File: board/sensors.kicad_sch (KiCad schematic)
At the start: 9 parts, among them J7 U.FL GPS, U7 MAX-M10M

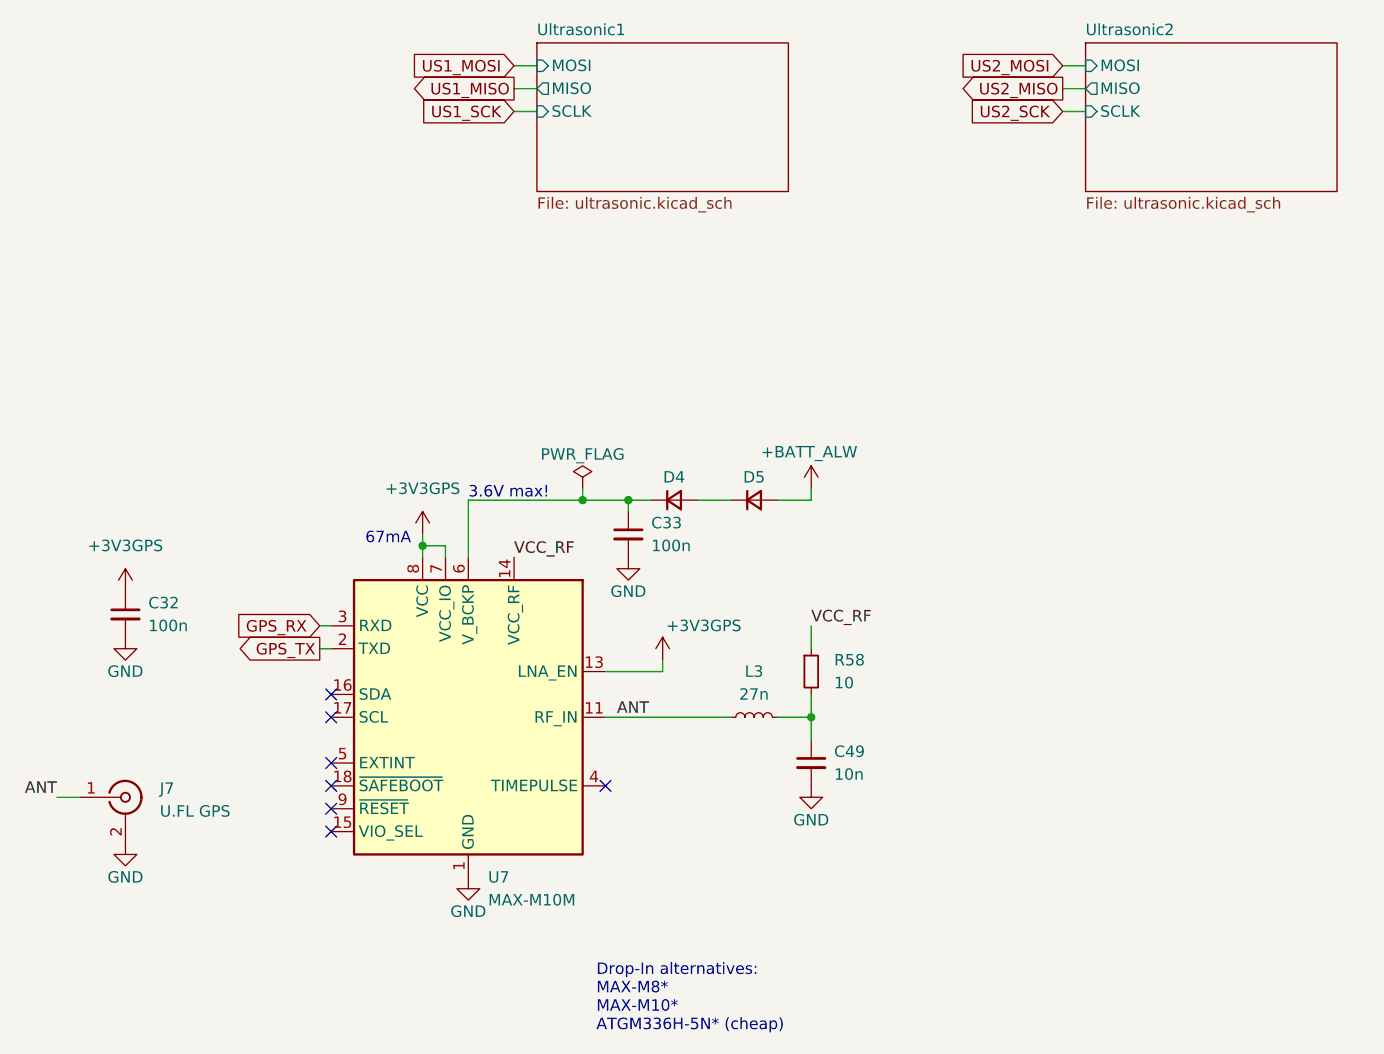
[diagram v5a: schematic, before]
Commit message: Update schematic and PCB layout
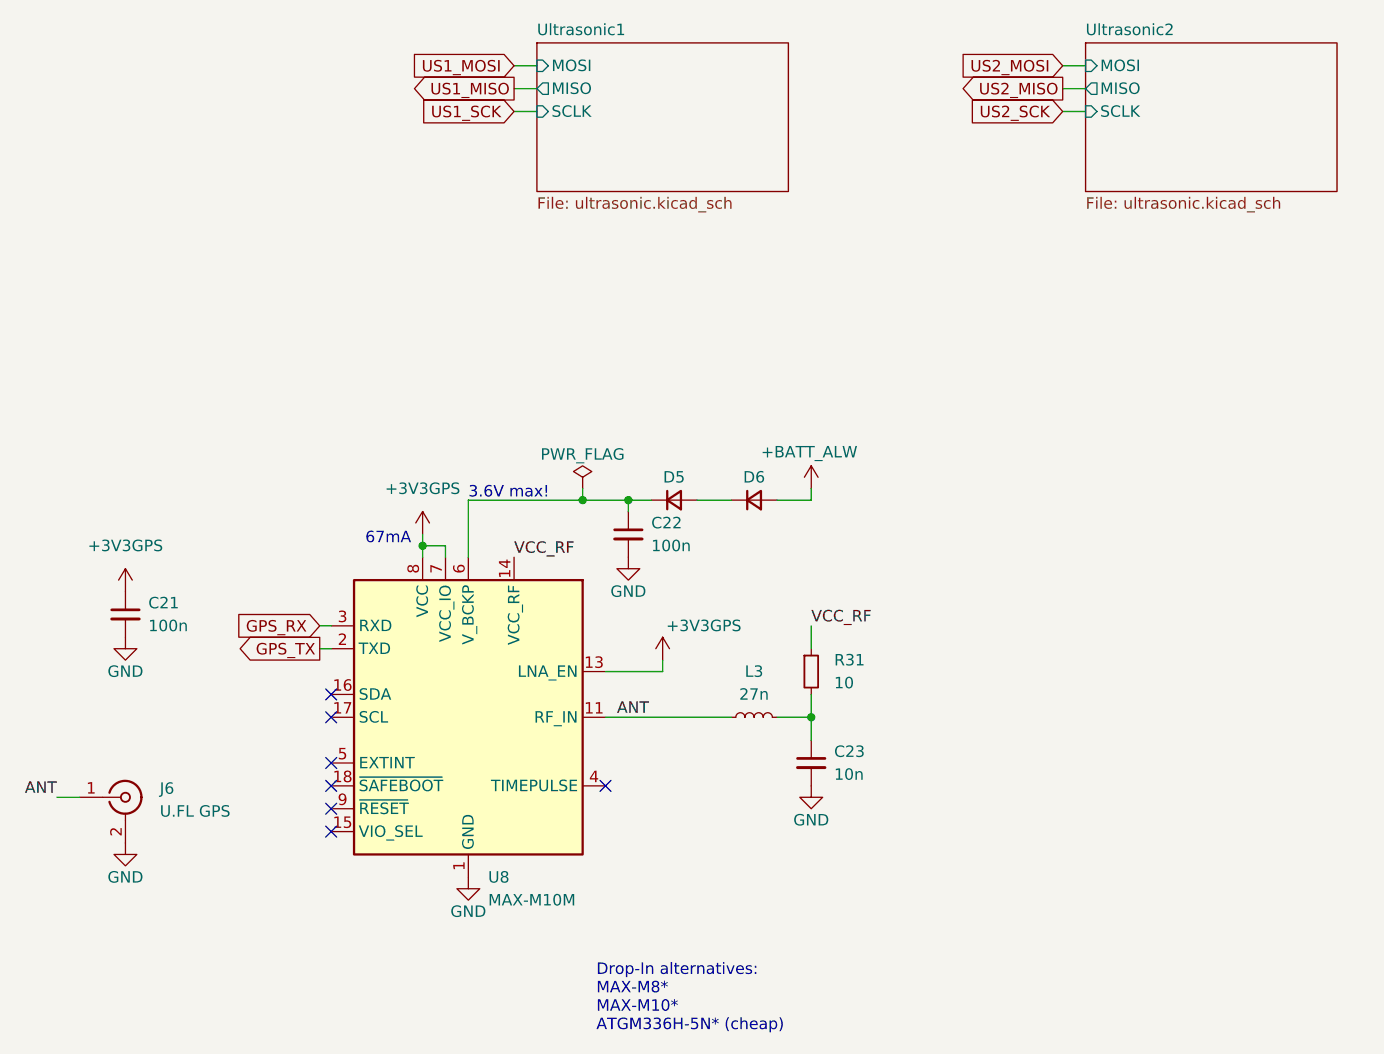
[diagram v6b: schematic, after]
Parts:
- renumbered C32 to C21, C33 to C22, C49 to C23, D4 to D5, D5 to D6, J7 to J6, R58 to R31, U7 to U8
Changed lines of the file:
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@@
 		(dnp no)
 		(fields_autoplaced yes)
-		(property "Reference" "#PWR092"
+		(property "Reference" "#PWR070"
 			(at 85.09 104.14 0)
 			(effects
@@
 			(project "OBSPro"
 				(path "/1b575199-a76e-4620-8a1a-43f78ed7da24/92aed634-9154-4b6d-b7ec-aef540896df2"
-					(reference "#PWR092")
+					(reference "#PWR070")
 					(unit 1)
 				)
@@
 		(on_board yes)
 		(dnp no)
-		(property "Reference" "D4"
+		(property "Reference" "D5"
 			(at 90.17 88.9 0)
 			(effects
@@
 			(project "OBSPro"
 				(path "/1b575199-a76e-4620-8a1a-43f78ed7da24/92aed634-9154-4b6d-b7ec-aef540896df2"
-					(reference "D4")
+					(reference "D5")
 					(unit 1)
 				)
@@
 		(dnp no)
 		(fields_autoplaced yes)
-		(property "Reference" "#PWR091"
+		(property "Reference" "#PWR066"
 			(at 29.21 113.03 0)
 			(effects
@@
 			(project "OBSPro"
 				(path "/1b575199-a76e-4620-8a1a-43f78ed7da24/92aed634-9154-4b6d-b7ec-aef540896df2"
-					(reference "#PWR091")
+					(reference "#PWR066")
 					(unit 1)
 				)
@@
 		(dnp no)
 		(fields_autoplaced yes)
-		(property "Reference" "C49"
+		(property "Reference" "C23"
 			(at 107.95 119.3862 0)
 			(effects
@@
 			(project "OBSPro"
 				(path "/1b575199-a76e-4620-8a1a-43f78ed7da24/92aed634-9154-4b6d-b7ec-aef540896df2"
-					(reference "C49")
+					(reference "C23")
 					(unit 1)
 				)
@@
 		(dnp no)
 		(fields_autoplaced yes)
-		(property "Reference" "#PWR088"
+		(property "Reference" "#PWR065"
 			(at 29.21 105.41 0)
 			(effects
@@
 			(project "OBSPro"
 				(path "/1b575199-a76e-4620-8a1a-43f78ed7da24/92aed634-9154-4b6d-b7ec-aef540896df2"
-					(reference "#PWR088")
+					(reference "#PWR065")
 					(unit 1)
 				)
@@
 		(dnp no)
 		(fields_autoplaced yes)
-		(property "Reference" "U7"
+		(property "Reference" "U8"
 			(at 69.5041 133.35 0)
 			(effects
@@
 			(project "OBSPro"
 				(path "/1b575199-a76e-4620-8a1a-43f78ed7da24/92aed634-9154-4b6d-b7ec-aef540896df2"
-					(reference "U7")
+					(reference "U8")
 					(unit 1)
 				)
@@
 		(dnp no)
 		(fields_autoplaced yes)
-		(property "Reference" "C32"
+		(property "Reference" "C21"
 			(at 31.75 102.8762 0)
 			(effects
@@
 			(project "OBSPro"
 				(path "/1b575199-a76e-4620-8a1a-43f78ed7da24/92aed634-9154-4b6d-b7ec-aef540896df2"
-					(reference "C32")
+					(reference "C21")
 					(unit 1)
 				)
@@
 		(dnp no)
 		(fields_autoplaced yes)
-		(property "Reference" "J7"
+		(property "Reference" "J6"
 			(at 33.02 123.4831 0)
 			(effects
@@
 			(project "OBSPro"
 				(path "/1b575199-a76e-4620-8a1a-43f78ed7da24/92aed634-9154-4b6d-b7ec-aef540896df2"
-					(reference "J7")
+					(reference "J6")
 					(unit 1)
 				)
@@
 		(on_board yes)
 		(dnp no)
-		(property "Reference" "#PWR0102"
+		(property "Reference" "#PWR071"
 			(at 88.9 113.03 0)
 			(effects
@@
 			(project "OBSPro"
 				(path "/1b575199-a76e-4620-8a1a-43f78ed7da24/92aed634-9154-4b6d-b7ec-aef540896df2"
-					(reference "#PWR0102")
+					(reference "#PWR071")
 					(unit 1)
 				)
@@
 		(dnp no)
 		(fields_autoplaced yes)
-		(property "Reference" "#PWR093"
+		(property "Reference" "#PWR069"
 			(at 67.31 139.7 0)
 			(effects
@@
 			(project "OBSPro"
 				(path "/1b575199-a76e-4620-8a1a-43f78ed7da24/92aed634-9154-4b6d-b7ec-aef540896df2"
-					(reference "#PWR093")
+					(reference "#PWR069")
 					(unit 1)
 				)
@@
 		(dnp no)
 		(fields_autoplaced yes)
-		(property "Reference" "C33"
+		(property "Reference" "C22"
 			(at 87.63 93.9862 0)
 			(effects
@@
 			(project "OBSPro"
 				(path "/1b575199-a76e-4620-8a1a-43f78ed7da24/92aed634-9154-4b6d-b7ec-aef540896df2"
-					(reference "C33")
+					(reference "C22")
 					(unit 1)
 				)
@@
 		(dnp no)
 		(fields_autoplaced yes)
-		(property "Reference" "#PWR043"
+		(property "Reference" "#PWR073"
 			(at 105.41 129.54 0)
 			(effects
@@
 			(project "OBSPro"
 				(path "/1b575199-a76e-4620-8a1a-43f78ed7da24/92aed634-9154-4b6d-b7ec-aef540896df2"
-					(reference "#PWR043")
+					(reference "#PWR073")
 					(unit 1)
 				)
@@
 		(on_board yes)
 		(dnp no)
-		(property "Reference" "D5"
+		(property "Reference" "D6"
 			(at 99.06 88.9 0)
 			(effects
@@
 			(project "OBSPro"
 				(path "/1b575199-a76e-4620-8a1a-43f78ed7da24/92aed634-9154-4b6d-b7ec-aef540896df2"
-					(reference "D5")
+					(reference "D6")
 					(unit 1)
 				)
@@
 		(dnp no)
 		(fields_autoplaced yes)
-		(property "Reference" "#PWR042"
+		(property "Reference" "#PWR067"
 			(at 29.21 135.89 0)
 			(effects
@@
 			(project "OBSPro"
 				(path "/1b575199-a76e-4620-8a1a-43f78ed7da24/92aed634-9154-4b6d-b7ec-aef540896df2"
-					(reference "#PWR042")
+					(reference "#PWR067")
 					(unit 1)
 				)
@@
 		(on_board yes)
 		(dnp no)
-		(property "Reference" "#PWR090"
+		(property "Reference" "#PWR072"
 			(at 105.41 93.98 0)
 			(effects
@@
 			(project "OBSPro"
 				(path "/1b575199-a76e-4620-8a1a-43f78ed7da24/92aed634-9154-4b6d-b7ec-aef540896df2"
-					(reference "#PWR090")
+					(reference "#PWR072")
 					(unit 1)
 				)
@@
 		(dnp no)
 		(fields_autoplaced yes)
-		(property "Reference" "R58"
+		(property "Reference" "R31"
 			(at 107.95 109.22 0)
 			(effects
@@
 			(project "OBSPro"
 				(path "/1b575199-a76e-4620-8a1a-43f78ed7da24/92aed634-9154-4b6d-b7ec-aef540896df2"
-					(reference "R58")
+					(reference "R31")
 					(unit 1)
 				)
@@
 		(dnp no)
 		(fields_autoplaced yes)
-		(property "Reference" "#PWR089"
+		(property "Reference" "#PWR068"
 			(at 62.23 99.06 0)
 			(effects
@@
 			(project "OBSPro"
 				(path "/1b575199-a76e-4620-8a1a-43f78ed7da24/92aed634-9154-4b6d-b7ec-aef540896df2"
-					(reference "#PWR089")
+					(reference "#PWR068")
 					(unit 1)
 				)
@@
 		(on_board yes)
 		(dnp no)
-		(property "Reference" "#FLG07"
+		(property "Reference" "#FLG08"
 			(at 80.01 88.265 0)
 			(effects
@@
 			(project "OBSPro"
 				(path "/1b575199-a76e-4620-8a1a-43f78ed7da24/92aed634-9154-4b6d-b7ec-aef540896df2"
-					(reference "#FLG07")
+					(reference "#FLG08")
 					(unit 1)
 				)

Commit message: Various PCB tweaks, add power LED, add BOOT button
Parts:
- C21, C22: JLC_BasicPart yes -> (none); JLC_Price1 0.042 -> (none); JLC_Price10 0.0021 -> (none); JLC_Price100 0.0021 -> (none); JLC_Price1000 0.0014 -> (none); PCBA yes -> (none); kicost:JLC:pricing 1: USD 0.0020; 200: USD 0.0016; 800: USD 0.0013; 1600: USD 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 -> (none)
- D5, D6: JLC_BasicPart yes -> (none); JLC_Price10 0.0064 -> (none); PCBA yes -> (none); kicost:JLC:pricing 1: USD 0.0137; 50: USD 0.0111; 150: USD 0.0097; 500: USD 0.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 -> (none)
- R31: JLC_BasicPart no -> (none)
- U8: JLC_BasicPart no -> (none); JLC_Price1 21.0 -> (none); JLC_Price10 15.07 -> (none); JLC_Price100 10.32 -> (none); JLC_Price1000 10.32 -> (none); PCBA no -> (none); kicost:JLC:pricing 1: USD 21; 10: USD 15.73; 100: USD 10.32; 1000: USD 10.32 -> (none)
